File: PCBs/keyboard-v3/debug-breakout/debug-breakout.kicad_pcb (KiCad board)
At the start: 2 copper layers, 38 x 12 mm, 4 parts, among them J101 Conn_ST_STDC14, J102 Conn_ST_STDC14, J103 Conn_ST_STDC14, J501 Conn_02x08_Odd_Even

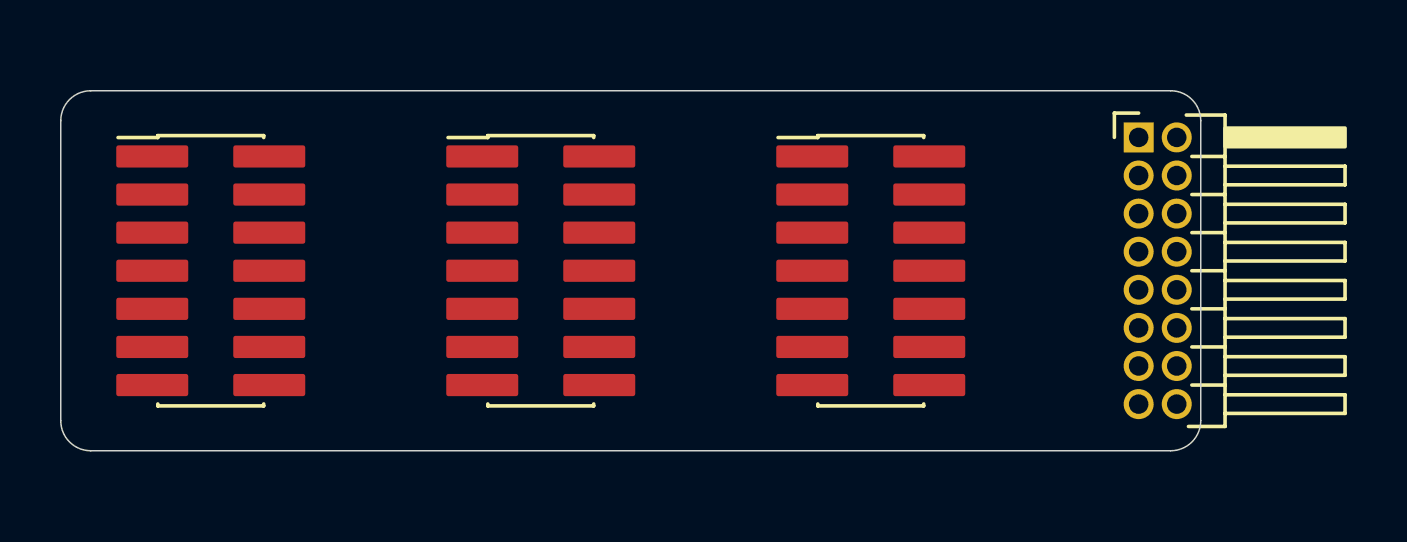
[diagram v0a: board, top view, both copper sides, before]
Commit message: Finished debug breakout board and added 5V voltage sensing to key board
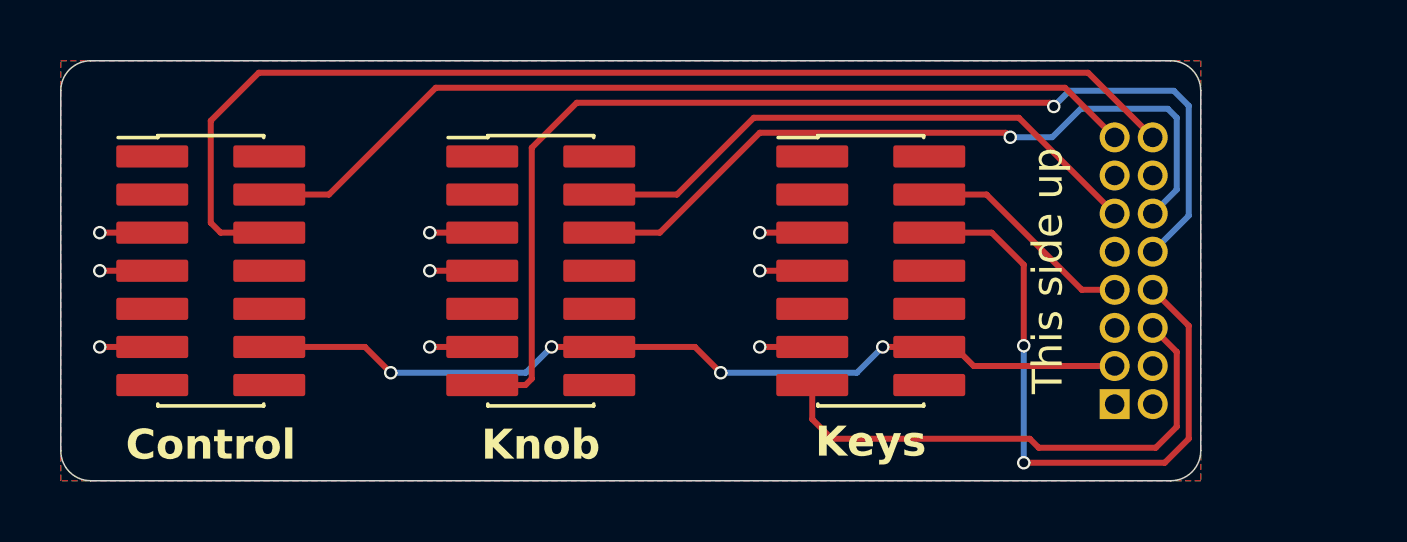
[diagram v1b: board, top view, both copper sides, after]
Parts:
- J501: moved to B.Cu
- moved J501 8.93 mm to (142.1, 96.4)
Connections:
- J501 pad 1: /CTRL.SWCLK -> +3V3
- J501 pad 10: /KEYS.SWDIO -> /KNOB.RX
- J501 pad 11: GND -> /KNOB.SWDIO
- J501 pad 12: /KEYS.RX -> /KNOB.SWCLK
- J501 pad 13: /~{RST} -> GND
- J501 pad 15: +3V3 -> /CTRL.SWDIO
- J501 pad 16: VBUS -> /CTRL.SWCLK
- J501 pad 2: /CTRL.SWDIO -> VBUS
- J501 pad 3: GND -> /~{RST}
- J501 pad 5: /KNOB.SWCLK -> GND
- J501 pad 6: /KNOB.SWDIO -> /KEYS.RX
- J501 pad 7: GND -> /KEYS.SWDIO
- J501 pad 8: /KNOB.RX -> /KEYS.SWCLK
- J501 pad 9: /KEYS.SWCLK -> GND
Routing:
- net /CTRL.SWCLK: track 0.00 -> 38.4 mm
- net /KNOB.RX: track 0.00 -> 37.8 mm, vias 0 -> 1
- net /CTRL.SWDIO: track 0.00 -> 30.3 mm
- net /~{RST}: track 0.00 -> 29.9 mm, vias 0 -> 4
- net /KNOB.SWCLK: track 0.00 -> 24.7 mm, vias 0 -> 1
- net /KEYS.SWCLK: track 0.00 -> 21.5 mm, vias 0 -> 2
- net /KNOB.SWDIO: track 0.00 -> 19.6 mm
- net /KEYS.RX: track 0.00 -> 17.6 mm
- net GND: track 0.00 -> 15.8 mm, vias 0 -> 9
- net /KEYS.SWDIO: track 0.00 -> 7.50 mm
- added copper zone on F.Cu, net +3V3
- added copper zone on B.Cu, net GND
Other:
- board size 38 x 12 mm -> 38 x 14 mm
- board text added: "1.0.0"
- board text added: "Control"
- board text added: "Designed by Ben Smith"
- board text added: "KEYBOARD V3 DEBUG"
- board text added: "Keys"
- board text added: "Knob"
- board text added: "This side up"

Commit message: Keyboard v3 hardware done
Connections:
- J501 pad 1: +3V3 -> VBUS
- J501 pad 10: /KNOB.RX -> GND
- J501 pad 11: /KNOB.SWDIO -> /KNOB.SWCLK
- J501 pad 12: /KNOB.SWCLK -> /KNOB.SWDIO
- J501 pad 15: /CTRL.SWDIO -> /CTRL.SWCLK
- J501 pad 16: /CTRL.SWCLK -> /CTRL.SWDIO
- J501 pad 2: VBUS -> +3V3
- J501 pad 3: /~{RST} -> GND
- J501 pad 4: GND -> /~{RST}
- J501 pad 5: GND -> /KEYS.RX
- J501 pad 6: /KEYS.RX -> GND
- J501 pad 7: /KEYS.SWDIO -> /KEYS.SWCLK
- J501 pad 8: /KEYS.SWCLK -> /KEYS.SWDIO
- J501 pad 9: GND -> /KNOB.RX
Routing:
- net /KEYS.SWCLK: track 21.5 -> 6.94 mm, vias 2 -> 0
- net /KEYS.SWDIO: track 7.50 -> 20.3 mm, vias 0 -> 2
- net /CTRL.SWCLK: track 38.4 -> 30.8 mm
- net GND: track 15.8 -> 23.2 mm, vias 9 -> 14
- net /~{RST}: track 29.9 -> 35.8 mm, vias 4 -> 5
- net /KNOB.SWDIO: track 19.6 -> 25.4 mm, vias 0 -> 2
- net /KNOB.SWCLK: track 24.7 -> 19.6 mm
- net /KNOB.RX: track 37.8 -> 32.7 mm, vias 1 -> 0
- net /KEYS.RX: track 17.6 -> 13.0 mm
- net /CTRL.SWDIO: track 30.3 -> 32.0 mm
